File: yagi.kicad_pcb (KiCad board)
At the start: 2 copper layers, 65 x 56 mm, 56 parts, among them IC1 AT24CS32-SSHM, J1 RPi_GPIO, P1 HV+, P2 HV-, P3 CONN_01X01, P4 CONN_01X01, P5 CONN_01X02, P6 CONN_01X03, P7 CONN_01X02, Q1 STN0214, Q2 STN0214, Q3 MMBT4401, U1 74LS244

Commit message: Finish layouting.
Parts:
- added P10: CONN_01X02, Pin_Headers:Pin_Header_Straight_1x02, F.Cu at (45.5, 80.0)
- added P11: CONN_01X02, Pin_Headers:Pin_Header_Straight_1x02, F.Cu at (64.5, 50.0)
- added P12: CONN_01X03, Pin_Headers:Pin_Header_Straight_1x03, F.Cu at (55.8, 53.0)
- added P8: CONN_01X03, Pin_Headers:Pin_Header_Straight_1x03, F.Cu at (41.5, 80.0)
- added P9: CONN_01X03, Pin_Headers:Pin_Header_Straight_1x03, F.Cu at (64.5, 54.0)
- added REF** (x4): SolderWirePad_single_0-8mmDrill, Wire_Pads:SolderWirePad_single_0-8mmDrill, F.Cu at (100.3, 81.3)
- added REF**: SolderWirePad_single_0-8mmDrill, Wire_Pads:SolderWirePad_single_0-8mmDrill, F.Cu at (97.8, 73.7)
- added REF**: SolderWirePad_single_0-8mmDrill, Wire_Pads:SolderWirePad_single_0-8mmDrill, F.Cu at (97.8, 76.2)
- added REF**: SolderWirePad_single_0-8mmDrill, Wire_Pads:SolderWirePad_single_0-8mmDrill, F.Cu at (97.8, 78.7)
- added REF**: SolderWirePad_single_0-8mmDrill, Wire_Pads:SolderWirePad_single_0-8mmDrill, F.Cu at (97.8, 81.3)
- added REF**: SolderWirePad_single_0-8mmDrill, Wire_Pads:SolderWirePad_single_0-8mmDrill, F.Cu at (95.2, 71.1)
- added REF**: SolderWirePad_single_0-8mmDrill, Wire_Pads:SolderWirePad_single_0-8mmDrill, F.Cu at (95.2, 73.7)
- added REF**: SolderWirePad_single_0-8mmDrill, Wire_Pads:SolderWirePad_single_0-8mmDrill, F.Cu at (95.2, 76.2)
- added REF**: SolderWirePad_single_0-8mmDrill, Wire_Pads:SolderWirePad_single_0-8mmDrill, F.Cu at (95.2, 78.7)
- added REF**: SolderWirePad_single_0-8mmDrill, Wire_Pads:SolderWirePad_single_0-8mmDrill, F.Cu at (95.2, 81.3)
- added REF**: SolderWirePad_single_0-8mmDrill, Wire_Pads:SolderWirePad_single_0-8mmDrill, F.Cu at (92.7, 71.1)
- added REF**: SolderWirePad_single_0-8mmDrill, Wire_Pads:SolderWirePad_single_0-8mmDrill, F.Cu at (100.3, 73.7)
- added REF**: SolderWirePad_single_0-8mmDrill, Wire_Pads:SolderWirePad_single_0-8mmDrill, F.Cu at (92.7, 73.7)
- added REF**: SolderWirePad_single_0-8mmDrill, Wire_Pads:SolderWirePad_single_0-8mmDrill, F.Cu at (90.2, 71.1)
- added REF**: SolderWirePad_single_0-8mmDrill, Wire_Pads:SolderWirePad_single_0-8mmDrill, F.Cu at (90.2, 73.7)
- added REF**: SolderWirePad_single_0-8mmDrill, Wire_Pads:SolderWirePad_single_0-8mmDrill, F.Cu at (87.6, 71.1)
- added REF**: SolderWirePad_single_0-8mmDrill, Wire_Pads:SolderWirePad_single_0-8mmDrill, F.Cu at (87.6, 73.7)
- added REF**: SolderWirePad_single_0-8mmDrill, Wire_Pads:SolderWirePad_single_0-8mmDrill, F.Cu at (87.6, 76.2)
- added REF**: SolderWirePad_single_0-8mmDrill, Wire_Pads:SolderWirePad_single_0-8mmDrill, F.Cu at (92.7, 76.2)
- added REF**: SolderWirePad_single_0-8mmDrill, Wire_Pads:SolderWirePad_single_0-8mmDrill, F.Cu at (90.2, 76.2)
- added REF**: SolderWirePad_single_0-8mmDrill, Wire_Pads:SolderWirePad_single_0-8mmDrill, F.Cu at (87.6, 78.7)
- added REF**: SolderWirePad_single_0-8mmDrill, Wire_Pads:SolderWirePad_single_0-8mmDrill, F.Cu at (90.2, 78.7)
- added REF**: SolderWirePad_single_0-8mmDrill, Wire_Pads:SolderWirePad_single_0-8mmDrill, F.Cu at (92.7, 78.7)
- added REF**: SolderWirePad_single_0-8mmDrill, Wire_Pads:SolderWirePad_single_0-8mmDrill, F.Cu at (92.7, 81.3)
- added REF**: SolderWirePad_single_0-8mmDrill, Wire_Pads:SolderWirePad_single_0-8mmDrill, F.Cu at (90.2, 81.3)
- added REF**: SolderWirePad_single_0-8mmDrill, Wire_Pads:SolderWirePad_single_0-8mmDrill, F.Cu at (87.6, 81.3)
- added REF**: SolderWirePad_single_0-8mmDrill, Wire_Pads:SolderWirePad_single_0-8mmDrill, F.Cu at (87.6, 83.8)
- added REF**: SolderWirePad_single_0-8mmDrill, Wire_Pads:SolderWirePad_single_0-8mmDrill, F.Cu at (90.2, 83.8)
- added REF**: SolderWirePad_single_0-8mmDrill, Wire_Pads:SolderWirePad_single_0-8mmDrill, F.Cu at (92.7, 83.8)
- added REF**: SolderWirePad_single_0-8mmDrill, Wire_Pads:SolderWirePad_single_0-8mmDrill, F.Cu at (95.2, 83.8)
- added REF**: SolderWirePad_single_0-8mmDrill, Wire_Pads:SolderWirePad_single_0-8mmDrill, F.Cu at (95.2, 86.4)
- added REF**: SolderWirePad_single_0-8mmDrill, Wire_Pads:SolderWirePad_single_0-8mmDrill, F.Cu at (92.7, 86.4)
- added REF**: SolderWirePad_single_0-8mmDrill, Wire_Pads:SolderWirePad_single_0-8mmDrill, F.Cu at (90.2, 86.4)
- added REF**: SolderWirePad_single_0-8mmDrill, Wire_Pads:SolderWirePad_single_0-8mmDrill, F.Cu at (87.6, 86.4)
- added REF**: SolderWirePad_single_0-8mmDrill, Wire_Pads:SolderWirePad_single_0-8mmDrill, F.Cu at (87.6, 88.9)
- added REF**: SolderWirePad_single_0-8mmDrill, Wire_Pads:SolderWirePad_single_0-8mmDrill, F.Cu at (90.2, 88.9)
- added REF**: SolderWirePad_single_0-8mmDrill, Wire_Pads:SolderWirePad_single_0-8mmDrill, F.Cu at (92.7, 88.9)
- added REF**: SolderWirePad_single_0-8mmDrill, Wire_Pads:SolderWirePad_single_0-8mmDrill, F.Cu at (95.2, 88.9)
- added REF**: SolderWirePad_single_0-8mmDrill, Wire_Pads:SolderWirePad_single_0-8mmDrill, F.Cu at (100.3, 71.1)
- added REF**: SolderWirePad_single_0-8mmDrill, Wire_Pads:SolderWirePad_single_0-8mmDrill, F.Cu at (100.3, 76.2)
- added REF**: SolderWirePad_single_0-8mmDrill, Wire_Pads:SolderWirePad_single_0-8mmDrill, F.Cu at (100.3, 78.7)
- added REF**: SolderWirePad_single_0-8mmDrill, Wire_Pads:SolderWirePad_single_0-8mmDrill, F.Cu at (97.8, 71.1)
- moved R5 2.42 mm to (46.7, 57.1), turned to 90 degrees
- moved C3 0.59 mm to (47.0, 52.2), turned to 180 degrees
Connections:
- J1 pad 10: (no net) -> Net-(J1-Pad10)
- J1 pad 11: (no net) -> Net-(J1-Pad11)
- J1 pad 13: (no net) -> Net-(J1-Pad13)
- J1 pad 15: (no net) -> Net-(J1-Pad15)
- J1 pad 17: (no net) -> Net-(J1-Pad17)
- J1 pad 19: (no net) -> Net-(J1-Pad19)
- J1 pad 20: (no net) -> Net-(J1-Pad20)
- J1 pad 21: (no net) -> Net-(J1-Pad21)
- J1 pad 22: (no net) -> Net-(J1-Pad22)
- J1 pad 23: (no net) -> Net-(J1-Pad23)
- J1 pad 24: (no net) -> Net-(J1-Pad24)
- J1 pad 25: (no net) -> Net-(J1-Pad25)
- J1 pad 26: (no net) -> Net-(J1-Pad26)
- J1 pad 29: (no net) -> Net-(J1-Pad29)
- J1 pad 3: (no net) -> Net-(J1-Pad3)
- J1 pad 30: (no net) -> Net-(J1-Pad30)
- J1 pad 31: (no net) -> Net-(J1-Pad31)
- J1 pad 33: (no net) -> Net-(J1-Pad33)
- J1 pad 34: (no net) -> Net-(J1-Pad34)
- J1 pad 35: (no net) -> Net-(J1-Pad35)
- J1 pad 37: (no net) -> Net-(J1-Pad37)
- J1 pad 39: (no net) -> Net-(J1-Pad39)
- J1 pad 5: (no net) -> Net-(J1-Pad5)
- J1 pad 7: (no net) -> Net-(J1-Pad7)
- J1 pad 8: (no net) -> Net-(J1-Pad8)
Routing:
- net Net-(J1-Pad8): track 0.00 -> 51.0 mm
- net Net-(J1-Pad10): track 0.00 -> 48.9 mm
- net Net-(J1-Pad7): track 0.00 -> 46.7 mm
- net Net-(J1-Pad5): track 0.00 -> 42.1 mm
- net Net-(J1-Pad3): track 0.00 -> 39.4 mm
- net Net-(J1-Pad21): track 0.00 -> 26.4 mm, vias 0 -> 1
- net Net-(J1-Pad26): track 0.00 -> 25.2 mm, vias 0 -> 1
- net Net-(J1-Pad19): track 0.00 -> 23.4 mm, vias 0 -> 1
- net Net-(J1-Pad24): track 0.00 -> 20.4 mm, vias 0 -> 2
- net Net-(J1-Pad23): track 0.00 -> 19.6 mm, vias 0 -> 1
- net GND: track 257.1 -> 247.2 mm, vias 9 -> 20
- net +3V3: track 79.6 -> 87.9 mm, vias 5 -> 6
- net +5V: track 36.3 -> 41.4 mm
- net Net-(C5-Pad1): track 3.93 -> 8.50 mm
- net Net-(P1-Pad1): track 0.00 -> 3.56 mm
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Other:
- board text added: "HV+"
- board text added: "HV-"
- board text added: "schroedingerskitten, yagi v0.1, 2015"

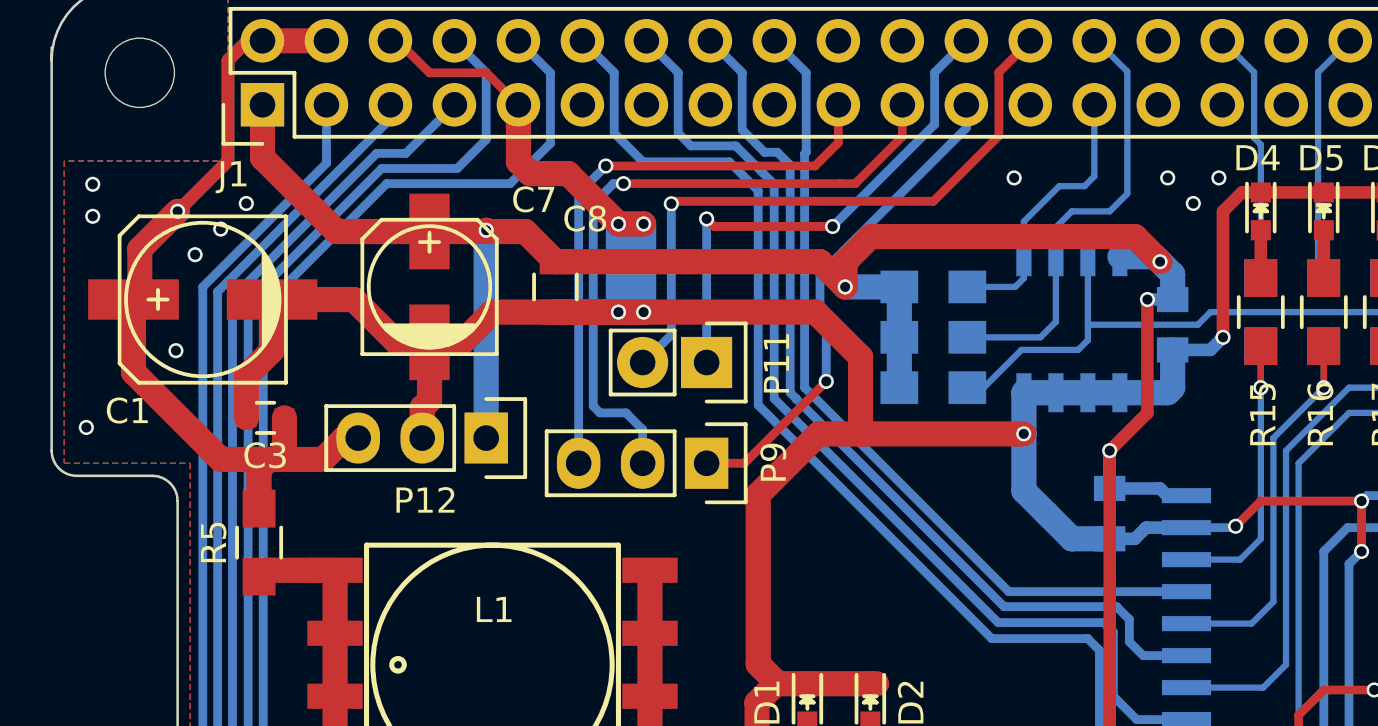
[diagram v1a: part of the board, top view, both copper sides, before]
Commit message: Add pins for easy current measurement for coil.
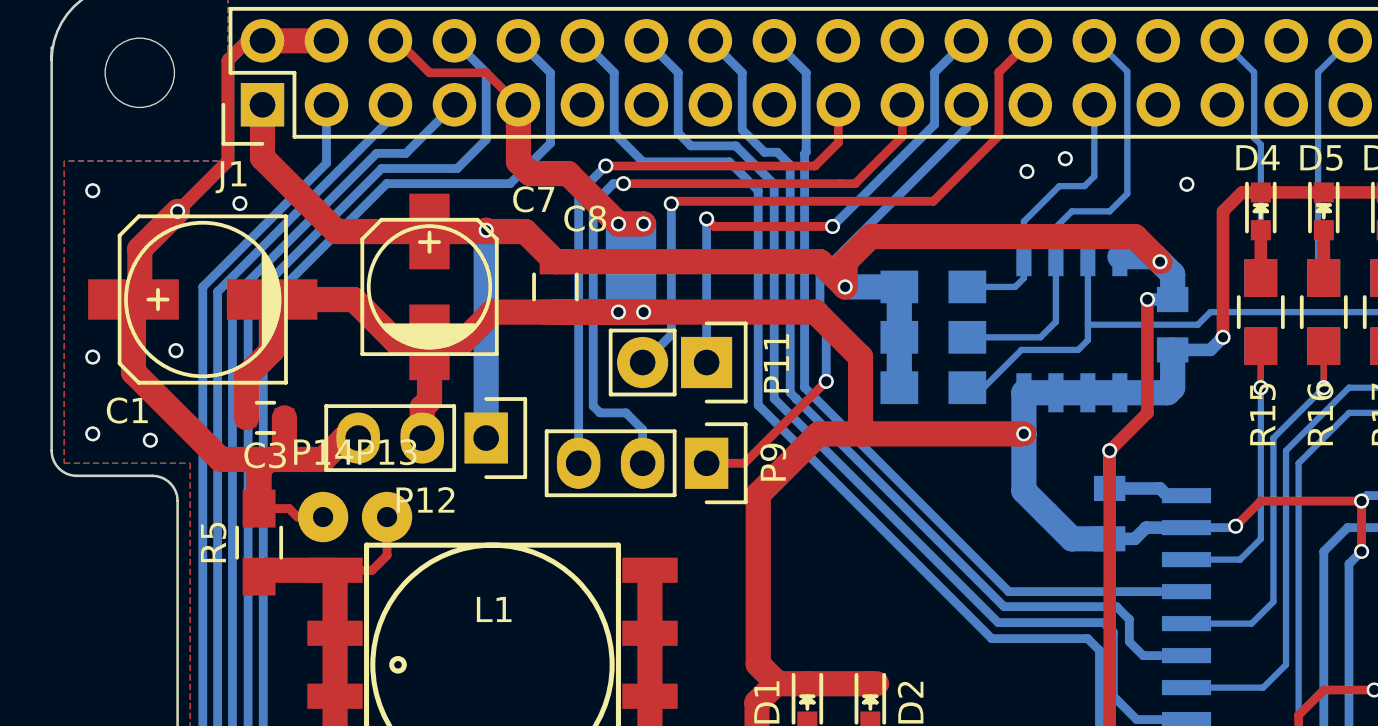
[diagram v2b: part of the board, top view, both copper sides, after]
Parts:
- added P13: CONN_01X01, Wire_Pads:SolderWirePad_single_0-8mmDrill, F.Cu at (51.8, 56.1)
- added P14: CONN_01X01, Wire_Pads:SolderWirePad_single_0-8mmDrill, F.Cu at (49.3, 56.1)
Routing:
- net Net-(L1-Pad1): track 10.6 -> 14.5 mm
- net +5V: track 41.4 -> 44.1 mm
- net GND: vias 20 -> 18
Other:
- net class Default: trace_width 1 -> 0.35
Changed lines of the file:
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@@
 (kicad_pcb (version 4) (host pcbnew 0.201509131501+6189~30~ubuntu14.04.1-product)
   (general
-    (links 120)
+    (links 122)
     (no_connects 2)
-    (area 28.003572 23.8 131.246429 97.200001)
+    (area 38.449999 34.949999 103.550001 91.050001)
     (thickness 1.6)
     (drawings 36)
-    (tracks 494)
+    (tracks 498)
     (zones 0)
-    (modules 106)
+    (modules 108)
     (nets 68)
   )
@@
   )
   (setup
-    (last_trace_width 1)
+    (last_trace_width 0.35)
     (trace_clearance 0.2)
     (zone_clearance 0.508)
@@
   (net_class Default "This is the default net class."
     (clearance 0.2)
-    (trace_width 1)
+    (trace_width 0.35)
     (via_dia 0.6)
     (via_drill 0.4)
@@
     )
   )
+  (module Wire_Pads:SolderWirePad_single_0-8mmDrill (layer F.Cu)
+    (at 51.816 56.134)
+    (fp_text reference P13 (at 0 -2.54) (layer F.SilkS)
+      (effects (font (size 1 1) (thickness 0.15)))
+    )
+    (fp_text value CONN_01X01 (at 0 2.54) (layer F.Fab)
+      (effects (font (size 1 1) (thickness 0.15)))
+    )
+    (pad 1 thru_hole circle (at 0 0) (size 1.99898 1.99898) (drill 0.8001) (layers *.Cu *.Mask F.SilkS)
+      (net 3 "Net-(L1-Pad1)"))
+  )
+  (module Wire_Pads:SolderWirePad_single_0-8mmDrill (layer F.Cu)
+    (at 49.276 56.134)
+    (fp_text reference P14 (at 0 -2.54) (layer F.SilkS)
+      (effects (font (size 1 1) (thickness 0.15)))
+    )
+    (fp_text value CONN_01X01 (at 0 2.54) (layer F.Fab)
+      (effects (font (size 1 1) (thickness 0.15)))
+    )
+    (pad 1 thru_hole circle (at 0 0) (size 1.99898 1.99898) (drill 0.8001) (layers *.Cu *.Mask F.SilkS)
+      (net 5 +5V))
+  )
   (gr_text HV- (at 65.532 86.106) (layer F.SilkS)
     (effects (font (size 2 2) (thickness 0.3)))
@@
   (gr_line (start 41.5 91) (end 100.5 91) (angle 90) (layer Edge.Cuts) (width 0.1))
   (gr_line (start 103.5 37.5) (end 103.5 88) (angle 90) (layer Edge.Cuts) (width 0.1))
-  (via (at 39.878 52.578) (size 0.6) (drill 0.4) (layers F.Cu B.Cu) (net 1))
-  (via (at 40.132 44.196) (size 0.6) (drill 0.4) (layers F.Cu B.Cu) (net 1))
-  (via (at 40.132 42.926) (size 0.6) (drill 0.4) (layers F.Cu B.Cu) (net 1))
-  (via (at 83.82 43.688) (size 0.6) (drill 0.4) (layers F.Cu B.Cu) (net 1))
-  (via (at 84.836 42.672) (size 0.6) (drill 0.4) (layers F.Cu B.Cu) (net 1))
-  (via (at 82.804 42.672) (size 0.6) (drill 0.4) (layers F.Cu B.Cu) (net 1))
-  (via (at 76.708 42.672) (size 0.6) (drill 0.4) (layers F.Cu B.Cu) (net 1))
-  (via (at 45.212 44.704) (size 0.6) (drill 0.4) (layers F.Cu B.Cu) (net 1))
-  (via (at 46.228 43.688) (size 0.6) (drill 0.4) (layers F.Cu B.Cu) (net 1))
+  (via (at 42.418 53.086) (size 0.6) (drill 0.4) (layers F.Cu B.Cu) (net 1))
+  (via (at 40.132 49.784) (size 0.6) (drill 0.4) (layers F.Cu B.Cu) (net 1))
+  (via (at 40.132 52.832) (size 0.6) (drill 0.4) (layers F.Cu B.Cu) (net 1))
+  (via (at 40.132 43.18) (size 0.6) (drill 0.4) (layers F.Cu B.Cu) (net 1))
+  (via (at 45.974 43.688) (size 0.6) (drill 0.4) (layers F.Cu B.Cu) (net 1))
+  (via (at 78.74 41.91) (size 0.6) (drill 0.4) (layers F.Cu B.Cu) (net 1))
+  (via (at 77.216 42.418) (size 0.6) (drill 0.4) (layers F.Cu B.Cu) (net 1))
+  (via (at 83.566 42.926) (size 0.6) (drill 0.4) (layers F.Cu B.Cu) (net 1))
   (via (at 43.434 49.53) (size 0.6) (drill 0.4) (layers F.Cu B.Cu) (net 1))
-  (via (at 44.196 45.72) (size 0.6) (drill 0.4) (layers F.Cu B.Cu) (net 1))
   (segment (start 46.24 52.197) (end 46.24 50.534) (width 1) (layer F.Cu) (net 1))
   (segment (start 47.25082 49.52318) (end 47.25082 47.5) (width 1) (layer F.Cu) (net 1))
@@
   (segment (start 53 74.65) (end 53 77.35) (width 0.5) (layer F.Cu) (net 2))
   (segment (start 53 77.35) (end 53.15 77.5) (width 0.5) (layer F.Cu) (net 2))
+  (segment (start 49.75 58.25) (end 51.224 58.25) (width 0.35) (layer F.Cu) (net 3))
+  (segment (start 51.816 57.658) (end 51.816 56.134) (width 0.35) (layer F.Cu) (net 3))
+  (segment (start 51.224 58.25) (end 51.816 57.658) (width 0.35) (layer F.Cu) (net 3))
   (segment (start 49.75 58.25) (end 46.986 58.25) (width 1) (layer F.Cu) (net 3))
   (segment (start 46.986 58.25) (end 46.736 58.5) (width 1) (layer F.Cu) (net 3))
@@
   (segment (start 55.85 80) (end 59.698 80) (width 0.5) (layer F.Cu) (net 4))
   (segment (start 55.85 80) (end 55.85 77.5) (width 0.5) (layer F.Cu) (net 4))
+  (segment (start 49.276 56.134) (end 48.26 56.134) (width 0.35) (layer F.Cu) (net 5))
+  (segment (start 47.926 55.8) (end 46.736 55.8) (width 0.35) (layer F.Cu) (net 5))
+  (segment (start 48.26 56.134) (end 47.926 55.8) (width 0.35) (layer F.Cu) (net 5))
   (segment (start 47.74 52.197) (end 47.74 53.848) (width 1) (layer F.Cu) (net 5))
   (segment (start 47.752 53.721) (end 47.752 53.848) (width 1) (layer F.Cu) (net 5))

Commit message: New try.
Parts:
- removed REF** (x45): SolderWirePad_single_0-8mmDrill, Wire_Pads:SolderWirePad_single_0-8mmDrill
- added C10: 0.1uF, Capacitors_SMD:C_0603_HandSoldering, B.Cu at (43.8, 47.0)
- added C11: 0.1uF, Capacitors_SMD:C_0603_HandSoldering, B.Cu at (101.6, 50.8)
- added C12: 0.1uF, Capacitors_SMD:C_0603_HandSoldering, B.Cu at (56.3, 81.2)
- added D8: Led_Small, LEDs:LED-0603, F.Cu at (88.3, 65.4)
- added P15: CONN_01X02, Pin_Headers:Pin_Header_Straight_1x02, F.Cu at (99.7, 44.5)
- added P16: CONN_01X02, Pin_Headers:Pin_Header_Straight_1x02, F.Cu at (55.2, 43.8)
- added P17: CONN_01X02, Pin_Headers:Pin_Header_Straight_1x02, F.Cu at (78.1, 47.6)
- added Q4: MMBT4401, TO_SOT_Packages_SMD:SOT-23, B.Cu at (96.5, 57.1)
- added R23: R, Resistors_SMD:R_0805_HandSoldering, F.Cu at (83.8, 59.7)
- added R24: 1k, Resistors_SMD:R_0805_HandSoldering, B.Cu at (92.7, 52.1)
- added R25: 3.9k, Resistors_SMD:R_0805_HandSoldering, F.Cu at (81.3, 46.4)
- added R26: 3.9k, Resistors_SMD:R_0805_HandSoldering, F.Cu at (83.2, 46.4)
- added U2: 74LS244, Housings_SSOP:TSSOP-20_4.4x6.5mm_Pitch0.65mm, B.Cu at (74.3, 55.2)
- C1: value 220uF -> 1nF; footprint Capacitors_SMD:c_elec_6.3x7.7 -> Capacitors_SMD:C_0805_HandSoldering; moved to B.Cu
- C2: footprint Capacitors_SMD:C_0805 -> Capacitors_SMD:C_1210_HandSoldering
- C3: value 1uF -> 47nF; footprint Capacitors_SMD:C_0603 -> Capacitors_SMD:C_1210_HandSoldering
- C4: value 47nF -> 330pF; footprint Capacitors_SMD:C_0805 -> Capacitors_SMD:C_0603_HandSoldering
- C5: value 330pF -> 220uF; footprint Capacitors_SMD:C_0603 -> Capacitors_SMD:c_elec_6.3x7.7
- C6: value 0.1uF -> 22uF; footprint Capacitors_SMD:C_0805 -> Capacitors_SMD:c_elec_5x4.5; moved to F.Cu
- C7: value 22uF -> 1uF; footprint Capacitors_SMD:c_elec_5x4.5 -> Capacitors_SMD:C_0805_HandSoldering; moved to B.Cu
- C8: footprint Capacitors_SMD:C_0805 -> Capacitors_SMD:C_0805_HandSoldering; moved to B.Cu
- C9: footprint Capacitors_SMD:C_0805 -> Capacitors_SMD:C_0603_HandSoldering
- D1: value Led_Small -> 1N4148; footprint LEDs:LED-0603 -> Discret:DO-35
- D2: value Led_Small -> D; footprint LEDs:LED-0603 -> chenit:TUMD2SM
- D3: value RFU02VSM8STR -> Led_Small; footprint chenit:TUMD2SM -> LEDs:LED-0603
- L1: value 15mH -> SRR0908-Y
- P1: value HV+ -> CONN_01X03; footprint Wire_Pads:SolderWirePad_single_1-2mmDrill -> Pin_Headers:Pin_Header_Straight_1x03
- P11: value CONN_01X02 -> CONN_01X03; footprint Pin_Headers:Pin_Header_Straight_1x02 -> Pin_Headers:Pin_Header_Straight_1x03
- P13, P14: value CONN_01X01 -> CONN_01X03; footprint Wire_Pads:SolderWirePad_single_0-8mmDrill -> Pin_Headers:Pin_Header_Straight_1x03
- P2: value HV- -> CONN_01X01; footprint Wire_Pads:SolderWirePad_single_1-2mmDrill -> chenit:PIN
- P3: footprint Wire_Pads:SolderWirePad_single_0-8mmDrill -> chenit:PIN
- P4: value CONN_01X01 -> CONN_01X02; footprint Wire_Pads:SolderWirePad_single_0-8mmDrill -> Pin_Headers:Pin_Header_Straight_1x02
- P5: value CONN_01X02 -> HV+; footprint Pin_Headers:Pin_Header_Straight_1x02 -> Wire_Pads:SolderWirePad_single_1-2mmDrill
- P6: value CONN_01X03 -> CONN_01X02; footprint Pin_Headers:Pin_Header_Straight_1x03 -> Pin_Headers:Pin_Header_Straight_1x02
- P7: value CONN_01X02 -> HV-; footprint Pin_Headers:Pin_Header_Straight_1x02 -> Wire_Pads:SolderWirePad_single_1-2mmDrill
- P8, P9: value CONN_01X03 -> CONN_01X01; footprint Pin_Headers:Pin_Header_Straight_1x03 -> Wire_Pads:SolderWirePad_single_0-8mmDrill
- Q1: value STN0214 -> MMBT4401; footprint chenit:SOT223 -> TO_SOT_Packages_SMD:SOT-23; moved to B.Cu
- Q2: footprint chenit:SOT223 -> TO_SOT_Packages_SMD:SOT-223
- Q3: value MMBT4401 -> STN0214; footprint TO_SOT_Packages_SMD:SOT-23 -> TO_SOT_Packages_SMD:SOT-223
- R10, R7, R9: moved to B.Cu
- R12: value 1k -> R; moved to F.Cu
- R13, R14: value 3.9k -> 10k; moved to F.Cu
- R15, R16: value R -> 10k
- R17: value R -> 1.5k
- R18: value R -> 100k
- R19: value 10k -> 27k; moved to F.Cu
- R2: value R -> 220k
- R20, R21, R22: value 10k -> R; moved to F.Cu
- R3: value R -> RV-TG; footprint Resistors_SMD:R_0805_HandSoldering -> chenit:bourns-3361-p
- R6: value R -> 330R
- R8: value 10M -> R
- U1: value 74LS244 -> TLC555; footprint Housings_SOIC:SOIC-20_7.5x12.8mm_Pitch1.27mm -> Housings_SOIC:SOIC-8_3.9x4.9mm_Pitch1.27mm
- moved P5 66.5 mm to (41.9, 77.5)
- moved P8 55.2 mm to (92.1, 57.8)
- moved C4 50.3 mm to (99.1, 73.7)
- moved C1 41.1 mm to (53.3, 87.6)
- moved C5 40.2 mm to (49.5, 55.2), turned to 270 degrees
- moved R12 37.9 mm to (43.2, 73.7), turned to 180 degrees
- moved U1 34.3 mm to (61.6, 82.5)
- moved R10 31.9 mm to (65.4, 53.3), turned to 180 degrees
- moved P14 29.0 mm to (75.6, 43.8), turned to 270 degrees
- moved P10 29.0 mm to (67.3, 61.0), turned to 270 degrees
- moved R9 28.0 mm to (65.4, 55.2), turned to 180 degrees
- moved C6 27.5 mm to (56.5, 55.9)
- moved D6 27.1 mm to (65.4, 51.4), turned to 180 degrees
- moved C3 26.6 mm to (46.4, 78.7), turned to 270 degrees
- moved Q3 26.1 mm to (52.7, 80.6), turned to 180 degrees
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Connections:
- C1 pad 1: +5V -> Net-(C1-Pad1)
- C3 pad 1: +5V -> Net-(C3-Pad1)
- C5 pad 1: Net-(C5-Pad1) -> +5V
- C7 pad 1: +3V3 -> +5V
- D1 pad 1: GND -> Net-(C1-Pad1)
- D2 pad 1: GND -> Net-(C2-Pad1)
- D3 pad 1: Net-(C2-Pad1) -> GND
- J1 pad 17: Net-(J1-Pad17) -> (no net)
- J1 pad 20: Net-(J1-Pad20) -> (no net)
- J1 pad 22: Net-(J1-Pad22) -> (no net)
- J1 pad 25: Net-(J1-Pad25) -> (no net)
- J1 pad 29: Net-(J1-Pad29) -> (no net)
- J1 pad 30: Net-(J1-Pad30) -> (no net)
- J1 pad 31: Net-(J1-Pad31) -> (no net)
- J1 pad 33: Net-(J1-Pad33) -> (no net)
- J1 pad 34: Net-(J1-Pad34) -> (no net)
- J1 pad 35: Net-(J1-Pad35) -> (no net)
- J1 pad 37: Net-(J1-Pad37) -> (no net)
- J1 pad 39: Net-(J1-Pad39) -> (no net)
- L1 pad 1: Net-(L1-Pad1) -> +5V
- L1 pad 2: Net-(L1-Pad1) -> +5V
- L1 pad 3: Net-(L1-Pad1) -> +5V
- L1 pad 4: Net-(L1-Pad1) -> +5V
- L1 pad 5: Net-(D3-Pad2) -> Net-(D2-Pad2)
- L1 pad 6: Net-(D3-Pad2) -> Net-(D2-Pad2)
- L1 pad 7: Net-(D3-Pad2) -> Net-(D2-Pad2)
- L1 pad 8: Net-(D3-Pad2) -> Net-(D2-Pad2)
- P10 pad 1: Net-(J1-Pad8) -> (no net)
- P10 pad 2: Net-(J1-Pad10) -> TRG
- P11 pad 1: Net-(J1-Pad24) -> +3V3
- P11 pad 2: Net-(J1-Pad26) -> GND
- P12 pad 1: +3V3 -> Net-(J1-Pad7)
- P12 pad 2: GND -> Net-(J1-Pad5)
- P12 pad 3: +5V -> Net-(J1-Pad3)
- P13 pad 1: Net-(L1-Pad1) -> Net-(J1-Pad15)
- P14 pad 1: +5V -> Net-(J1-Pad23)
- P2 pad 1: Net-(C5-Pad1) -> RST
- P3 pad 1: Net-(P3-Pad1) -> TRG
- P4 pad 1: detect -> Net-(P4-Pad1)
- P5 pad 1: GND -> Net-(P5-Pad1)
- P7 pad 1: Net-(P7-Pad1) -> Net-(C4-Pad1)
- P8 pad 1: Net-(J1-Pad7) -> Net-(P8-Pad1)
- P9 pad 1: Net-(J1-Pad23) -> detect
- Q1 pad 2: Net-(D3-Pad2) -> GND
- Q1 pad 3: GND -> RST
- Q2 pad 1: Net-(Q2-Pad1) -> TRG
- Q2 pad 2: Net-(Q2-Pad2) -> Net-(D2-Pad2)
- Q2 pad 3: GND -> Net-(Q1-Pad1)
- Q2 pad 4: Net-(Q2-Pad2) -> Net-(D2-Pad2)
- Q3 pad 1: Net-(P3-Pad1) -> DISC
- Q3 pad 2: GND -> Net-(Q3-Pad2)
- Q3 pad 3: detect -> GND
- R1 pad 1: Net-(D1-Pad2) -> +5V
- R1 pad 2: pulse -> RST
- R10 pad 1: GND -> Net-(R10-Pad1)
- R10 pad 2: Net-(P3-Pad1) -> Net-(D5-Pad2)
- R11 pad 1: detect -> Net-(R11-Pad1)
- R11 pad 2: +3V3 -> Net-(D6-Pad2)
- R12 pad 1: +3V3 -> Net-(C3-Pad1)
- R12 pad 2: Net-(IC1-Pad7) -> Net-(P5-Pad1)
- R13 pad 1: +3V3 -> DET
- R13 pad 2: ID_SD -> Net-(R13-Pad2)
- R14 pad 1: +3V3 -> AUX_IN1
- R14 pad 2: ID_SC -> Net-(R14-Pad2)
- R15 pad 1: Net-(R15-Pad1) -> AUX_IN2
- R15 pad 2: Net-(D4-Pad2) -> Net-(R10-Pad1)
- R16 pad 1: Net-(R16-Pad1) -> AUX_IN3
- R16 pad 2: Net-(D5-Pad2) -> Net-(R11-Pad1)
- R17 pad 1: Net-(R17-Pad1) -> Net-(P8-Pad1)
- R17 pad 2: Net-(D6-Pad2) -> Net-(C4-Pad1)
- R18 pad 1: Net-(R18-Pad1) -> GND
- R18 pad 2: Net-(D7-Pad2) -> Net-(P8-Pad1)
- R19 pad 1: DET -> detect
- R19 pad 2: Net-(R15-Pad1) -> +3V3
- R2 pad 1: Net-(D2-Pad2) -> Net-(R2-Pad1)
- R2 pad 2: discharge -> GND
- R20 pad 1: AUX_IN1 -> Net-(D7-Pad2)
- R20 pad 2: Net-(R16-Pad1) -> pulse
- R21 pad 1: AUX_IN2 -> Net-(D8-Pad2)
- R21 pad 2: Net-(R17-Pad1) -> discharge
- R22 pad 1: AUX_IN3 -> (no net)
- R22 pad 2: Net-(R18-Pad1) -> pulse
- R3 pad 1: Net-(Q1-Pad1) -> GND
- R3 pad 2: pulse -> GND
- R4 pad 1: Net-(Q2-Pad1) -> Net-(Q1-Pad1)
- R4 pad 2: discharge -> GND
- R5 pad 1: Net-(L1-Pad1) -> Net-(Q3-Pad2)
- R5 pad 2: +5V -> Net-(C2-Pad1)
- R6 pad 1: Net-(Q2-Pad2) -> Net-(P4-Pad1)
- R6 pad 2: Net-(C2-Pad1) -> Net-(D1-Pad2)
- R7 pad 1: Net-(C4-Pad1) -> Net-(R13-Pad2)
- R7 pad 2: Net-(Q2-Pad2) -> Net-(D3-Pad2)
- R8 pad 1: Net-(C4-Pad1) -> Net-(C3-Pad1)
- R8 pad 2: Net-(P1-Pad1) -> Net-(Q3-Pad2)
- R9 pad 1: Net-(P3-Pad1) -> Net-(R14-Pad2)
- R9 pad 2: Net-(C5-Pad1) -> Net-(D4-Pad2)
- U1 pad 2: detect -> Net-(R2-Pad1)
- U1 pad 3: Net-(P7-Pad2) -> Net-(D1-Pad2)
- U1 pad 4: Net-(P6-Pad3) -> RST
- U1 pad 5: Net-(P7-Pad1) -> (no net)
- U1 pad 6: Net-(P6-Pad2) -> GND
- U1 pad 7: discharge -> Net-(P4-Pad1)
- U1 pad 8: Net-(P6-Pad1) -> +5V
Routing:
- net +5V: track 44.1 -> 88.7 mm, vias 1 -> 6
- net Net-(J1-Pad8): track 51.0 -> 7.32 mm
- net Net-(R11-Pad1): track 0.00 -> 40.5 mm, vias 0 -> 1
- net Net-(J1-Pad10): track 48.9 -> 9.42 mm
- net DISC: track 40.5 -> 77.3 mm, vias 0 -> 5
- net Net-(R10-Pad1): track 0.00 -> 35.2 mm, vias 0 -> 1
- net Net-(J1-Pad7): track 46.7 -> 12.0 mm
- net Net-(J1-Pad5): track 42.1 -> 8.07 mm
- net Net-(R14-Pad2): track 0.00 -> 31.4 mm, vias 0 -> 1
- net Net-(J1-Pad3): track 39.4 -> 9.22 mm
- net +3V3: track 87.9 -> 117.1 mm, vias 6 -> 4
- net Net-(R18-Pad1): track 25.9 -> 0.00 mm, vias 1 -> 0
- net Net-(R13-Pad2): track 0.00 -> 25.5 mm, vias 0 -> 1
- net Net-(P4-Pad1): track 0.00 -> 24.6 mm, vias 0 -> 1
- net Net-(J1-Pad21): track 26.4 -> 4.36 mm, vias 1 -> 0
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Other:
- net class Default: trace_width 0.35 -> 1
- board text removed: "HV+"
- board text removed: "HV-"
